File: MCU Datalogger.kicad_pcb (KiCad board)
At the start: 2 copper layers, 50 x 30 mm, 29 parts, among them J1 Conn_01x09_Male, J2 Conn_01x04_Male, J3 Conn_02x03_Odd_Even, J4 Conn_01x04_Male, U1 24LC1025, U2 DS1337S+, U3 24LC1025, U4 ATMEGA328P-AU, Y1 32.768 KHz, Y2 16MHz

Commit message: more routing/wiring
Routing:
- net GND: track 51.7 -> 62.3 mm, vias 6 -> 10
- net /Vcc: track 93.1 -> 95.7 mm, vias 3 -> 5
- added copper zone on F.Cu, net /Vcc
- added copper zone on B.Cu, net GND
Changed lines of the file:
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@@
   (segment (start 108.3564 83.491) (end 110.1598 85.2944) (width 0.25) (layer "B.Cu") (net 1))
   (segment (start 110.1598 85.2944) (end 110.1598 88.2904) (width 0.25) (layer "B.Cu") (net 1))
-  (segment (start 116.120715 81.5594) (end 116.2793 81.5594) (width 0.35) (layer "F.Cu") (net 2))
   (segment (start 110.2716 77.724) (end 110.2716 78.6486) (width 0.35) (layer "F.Cu") (net 2))
   (segment (start 80.01 86.482) (end 81.031 87.503) (width 0.35) (layer "F.Cu") (net 2))
+  (segment (start 91.992 78.6892) (end 94.869 78.6892) (width 0.35) (layer "F.Cu") (net 2))
   (segment (start 98.7146 77.4446) (end 100.7262 77.4446) (width 0.35) (layer "F.Cu") (net 2))
   (segment (start 78.735489 85.207489) (end 78.735489 82.667489) (width 0.35) (layer "F.Cu") (net 2))
   (segment (start 116.2558 98.5012) (end 116.2558 98.0694) (width 0.35) (layer "F.Cu") (net 2))
   (segment (start 85.663 94.8436) (end 87.249 94.8436) (width 0.35) (layer "F.Cu") (net 2))
+  (segment (start 97.064178 86.303) (end 96.60003 86.767148) (width 0.35) (layer "F.Cu") (net 2))
   (segment (start 87.5792 78.6892) (end 91.992 78.6892) (width 0.35) (layer "F.Cu") (net 2))
   (segment (start 120.2417 81.1511) (end 119.2784 80.1878) (width 0.35) (layer "F.Cu") (net 2))
   (segment (start 84.792 78.6892) (end 87.5792 78.6892) (width 0.35) (layer "F.Cu") (net 2))
+  (segment (start 97.0382 87.903) (end 96.60003 87.46483) (width 0.35) (layer "F.Cu") (net 2))
   (segment (start 116.2793 81.5594) (end 116.2793 80.9987) (width 0.35) (layer "F.Cu") (net 2))
   (segment (start 116.2558 98.5012) (end 116.2558 94.2086) (width 0.35) (layer "F.Cu") (net 2))
-  (segment (start 91.992 78.6892) (end 97.3684 78.6892) (width 0.35) (layer "F.Cu") (net 2))
   (segment (start 91.8904 84.963) (end 90.5764 84.963) (width 0.35) (layer "F.Cu") (net 2))
   (segment (start 81.031 87.503) (end 84.6904 87.503) (width 0.35) (layer "F.Cu") (net 2))
   (segment (start 87.5792 78.784493) (end 87.5792 78.6892) (width 0.35) (layer "F.Cu") (net 2))
+  (segment (start 98.1382 86.303) (end 97.064178 86.303) (width 0.35) (layer "F.Cu") (net 2))
   (segment (start 97.3684 78.6892) (end 98.6638 77.3938) (width 0.35) (layer "F.Cu") (net 2))
   (segment (start 84.792 81.2292) (end 85.134493 81.2292) (width 0.35) (layer "F.Cu") (net 2))
@@
   (segment (start 80.01 86.482) (end 78.735489 85.207489) (width 0.35) (layer "F.Cu") (net 2))
   (segment (start 120.2417 81.5594) (end 120.2417 81.1511) (width 0.35) (layer "F.Cu") (net 2))
+  (segment (start 96.60003 86.767148) (end 96.60003 87.15123) (width 0.35) (layer "F.Cu") (net 2))
+  (segment (start 106.7382 87.103) (end 108.3882 87.103) (width 0.35) (layer "F.Cu") (net 2))
   (segment (start 87.249 94.8436) (end 87.4776 94.615) (width 0.35) (layer "F.Cu") (net 2))
   (segment (start 116.2558 94.2086) (end 116.1796 94.1324) (width 0.35) (layer "F.Cu") (net 2))
+  (segment (start 94.869 78.6892) (end 97.3684 78.6892) (width 0.35) (layer "F.Cu") (net 2))
   (segment (start 80.173778 81.2292) (end 84.792 81.2292) (width 0.35) (layer "F.Cu") (net 2))
   (segment (start 78.735489 82.667489) (end 80.173778 81.2292) (width 0.35) (layer "F.Cu") (net 2))
@@
   (segment (start 90.5764 84.963) (end 90.297 84.6836) (width 0.35) (layer "F.Cu") (net 2))
   (segment (start 100.7262 77.4446) (end 100.8024 77.3684) (width 0.35) (layer "F.Cu") (net 2))
+  (segment (start 94.869 78.6892) (end 94.869 78.7654) (width 0.35) (layer "F.Cu") (net 2))
+  (segment (start 96.60003 87.46483) (end 96.60003 87.15123) (width 0.35) (layer "F.Cu") (net 2))
+  (segment (start 94.869 78.7654) (end 95.504 79.4004) (width 0.35) (layer "F.Cu") (net 2))
   (segment (start 98.6638 77.3938) (end 98.7146 77.4446) (width 0.35) (layer "F.Cu") (net 2))
   (segment (start 116.2793 80.9987) (end 115.5446 80.264) (width 0.35) (layer "F.Cu") (net 2))
   (segment (start 85.134493 81.2292) (end 87.5792 78.784493) (width 0.35) (layer "F.Cu") (net 2))
+  (segment (start 108.3882 87.103) (end 108.585 87.2998) (width 0.35) (layer "F.Cu") (net 2))
+  (segment (start 98.1382 87.903) (end 97.0382 87.903) (width 0.35) (layer "F.Cu") (net 2))
+  (via (at 123.7742 94.5388) (size 0.9) (drill 0.4) (layers "F.Cu" "B.Cu") (net 2))
+  (via (at 96.60003 87.15123) (size 0.9) (drill 0.4) (layers "F.Cu" "B.Cu") (net 2))
   (via (at 117.4242 96.901) (size 0.9) (drill 0.4) (layers "F.Cu" "B.Cu") (net 2))
   (via (at 110.6424 79.0194) (size 0.9) (drill 0.4) (layers "F.Cu" "B.Cu") (net 2))
@@
   (via (at 115.5446 80.264) (size 0.9) (drill 0.4) (layers "F.Cu" "B.Cu") (net 2))
   (via (at 87.4776 94.615) (size 0.9) (drill 0.4) (layers "F.Cu" "B.Cu") (net 2))
+  (via (at 108.585 87.2998) (size 0.9) (drill 0.4) (layers "F.Cu" "B.Cu") (net 2))
   (via (at 119.2784 80.1878) (size 0.9) (drill 0.4) (layers "F.Cu" "B.Cu") (net 2))
+  (via (at 95.504 79.4004) (size 0.9) (drill 0.4) (layers "F.Cu" "B.Cu") (net 2))
+  (segment (start 126.4158 91.9734) (end 123.8504 94.5388) (width 0.35) (layer "B.Cu") (net 2))
+  (segment (start 123.8504 94.5388) (end 123.7742 94.5388) (width 0.35) (layer "B.Cu") (net 2))
   (segment (start 126.4158 94.5134) (end 126.3396 94.5134) (width 0.35) (layer "F.Cu") (net 3))
   (segment (start 87.10128 101.084795) (end 87.496405 101.47992) (width 0.35) (layer "F.Cu") (net 3))
@@
   (segment (start 122.047 88.5698) (end 120.8551 88.5698) (width 0.35) (layer "F.Cu") (net 3))
   (segment (start 88.3412 83.693) (end 91.8904 83.693) (width 0.35) (layer "F.Cu") (net 3))
+  (via (at 88.5444 79.9592) (size 0.8) (drill 0.4) (layers "F.Cu" "B.Cu") (free) (net 3))
   (via (at 123.571 90.0938) (size 0.9) (drill 0.4) (layers "F.Cu" "B.Cu") (net 3))
   (via (at 124.2822 92.456) (size 0.9) (drill 0.4) (layers "F.Cu" "B.Cu") (net 3))
   (via (at 119.1006 84.0994) (size 0.9) (drill 0.4) (layers "F.Cu" "B.Cu") (net 3))
+  (via (at 88.4428 77.47) (size 0.8) (drill 0.4) (layers "F.Cu" "B.Cu") (free) (net 3))
   (segment (start 105.3338 104.267) (end 106.557511 105.490711) (width 0.35) (layer "B.Cu") (net 3))
   (segment (start 125.115889 95.813311) (end 126.4158 94.5134) (width 0.35) (layer "B.Cu") (net 3))
   (segment (start 119.1006 84.0994) (end 121.528511 81.671489) (width 0.35) (layer "B.Cu") (net 3))
   (segment (start 115.326 104.2162) (end 116.600511 105.490711) (width 0.35) (layer "B.Cu") (net 3))
+  (segment (start 88.4428 77.47) (end 88.4428 79.8576) (width 0.35) (layer "B.Cu") (net 3))
   (segment (start 125.115889 101.629911) (end 125.115889 95.813311) (width 0.35) (layer "B.Cu") (net 3))
   (segment (start 114.051489 105.490711) (end 115.326 104.2162) (width 0.35) (layer "B.Cu") (net 3))
+  (segment (start 88.4428 79.8576) (end 88.5444 79.9592) (width 0.35) (layer "B.Cu") (net 3))
   (segment (start 116.600511 105.490711) (end 121.255089 105.490711) (width 0.35) (layer "B.Cu") (net 3))
   (segment (start 121.255089 105.490711) (end 125.115889 101.629911) (width 0.35) (layer "B.Cu") (net 3))
@@
   (segment (start 123.9978 82.946) (end 122.823289 84.120511) (width 0.25) (layer "B.Cu") (net 30))
   (segment (start 122.823289 89.596911) (end 121.8184 90.6018) (width 0.25) (layer "B.Cu") (net 30))
+  (zone (net 3) (net_name "/Vcc") (layer "F.Cu") (hatch edge 0.508)
+    (connect_pads (clearance 0.508))
+    (min_thickness 0.254) (filled_areas_thickness no)
+    (fill yes (thermal_gap 0.508) (thermal_bridge_width 0.508))
+    (polygon
+      (pts
+        (xy 123.825 78.3336)
+        (xy 123.9266 79.0448)
+        (xy 124.5362 80.0354)
+        (xy 125.603 80.518)
+        (xy 128.1938 80.4418)
+        (xy 128.1938 101.4476)
+        (xy 126.9492 101.5238)
+        (xy 125.7808 101.4476)
+        (xy 124.6886 101.7778)
+        (xy 123.698 102.8954)
+        (xy 123.4948 106.0196)
+        (xy 82.2706 106.0196)
+        (xy 82.6516 104.902)
+        (xy 82.931 104.0892)
+        (xy 82.8802 103.3018)
+        (xy 82.677 102.743)
+        (xy 82.2452 102.1334)
+        (xy 81.661 101.6762)
+        (xy 80.899 101.3968)
+        (xy 80.0354 101.4476)
+        (xy 78.3336 101.9556)
+        (xy 78.3336 81.7626)
+        (xy 78.359 79.9846)
+        (xy 79.4512 80.7974)
+        (xy 81.3816 80.772)
+        (xy 82.9564 79.375)
+        (xy 83.0326 76.2254)
+        (xy 83.0326 76.2508)
+        (xy 83.058 76.1492)
+        (xy 124.0028 76.1492)
+      )
+    )
+  )
+  (zone (net 2) (net_name "GND") (layer "B.Cu") (hatch edge 0.508)
+    (connect_pads (clearance 0.508))
+    (min_thickness 0.254) (filled_areas_thickness no)
+    (fill yes (thermal_gap 0.508) (thermal_bridge_width 0.508))
+    (polygon
+      (pts
+        (xy 123.825 78.3336)
+        (xy 123.9266 79.0448)
+        (xy 124.5362 80.0354)
+        (xy 125.603 80.518)
+        (xy 128.1938 80.4418)
+        (xy 128.1938 101.4476)
+        (xy 126.9492 101.5238)
+        (xy 125.7808 101.4476)
+        (xy 124.6886 101.7778)
+        (xy 123.698 102.8954)
+        (xy 123.4948 106.0196)
+        (xy 82.2706 106.0196)
+        (xy 82.6516 104.902)
+        (xy 82.931 104.0892)
+        (xy 82.8802 103.3018)
+        (xy 82.677 102.743)
+        (xy 82.2452 102.1334)
+        (xy 81.661 101.6762)
+        (xy 80.899 101.3968)
+        (xy 80.0354 101.4476)
+        (xy 78.3336 101.9556)
+        (xy 78.3336 81.7626)
+        (xy 78.359 79.9846)
+        (xy 79.4512 80.7974)
+        (xy 81.3816 80.772)
+        (xy 82.9564 79.375)
+        (xy 83.0326 76.2254)
+        (xy 83.0326 76.2508)
+        (xy 83.058 76.1492)
+        (xy 124.0028 76.1492)
+      )
+    )
+  )
 )

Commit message: completed routing
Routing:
- net GND: track 62.3 -> 58.6 mm, vias 10 -> 9
- net /Vcc: track 95.7 -> 97.1 mm

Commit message: ready to start on the silk screen
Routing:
- net /Vcc: track 97.1 -> 114.4 mm, vias 5 -> 6
- net /SDA: track 62.6 -> 63.9 mm
- net /D3: track 24.5 -> 25.2 mm

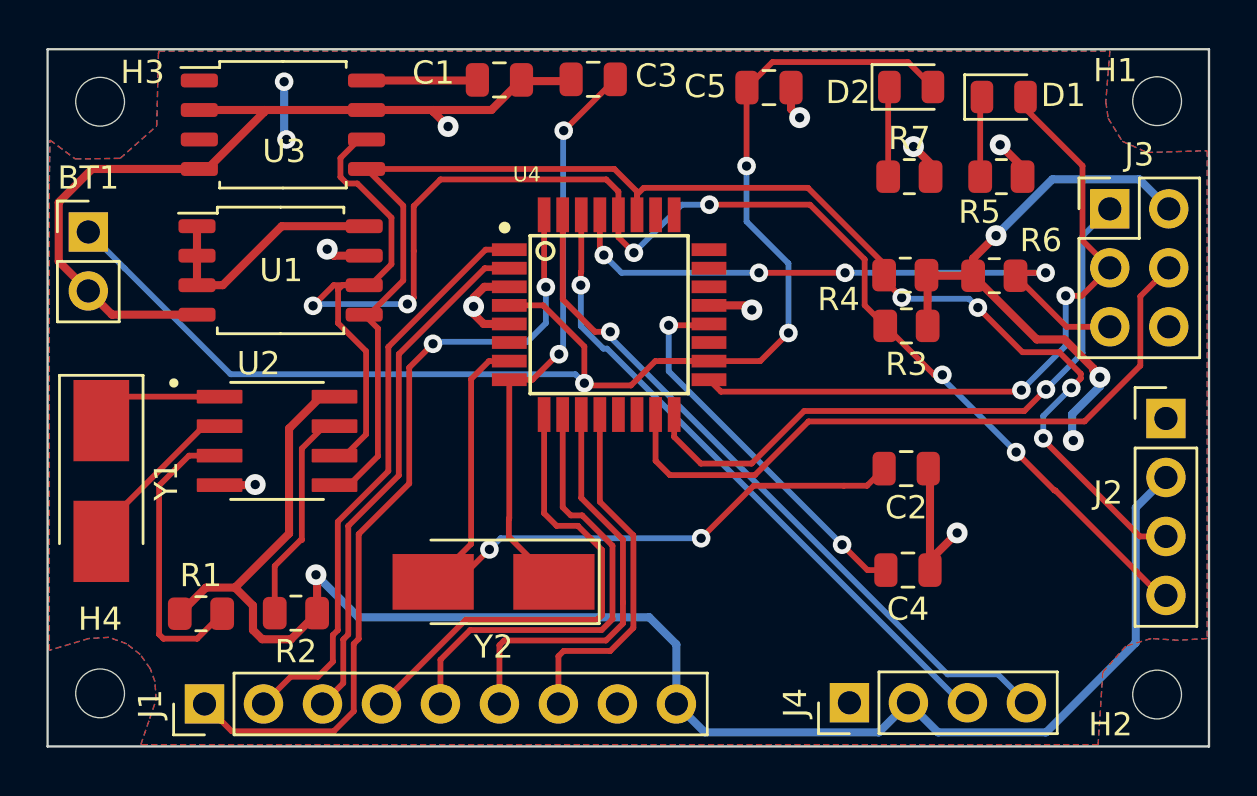
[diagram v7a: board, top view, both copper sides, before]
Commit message: Post fixing the schematic for the missing vcc net and the pcb resulting changes
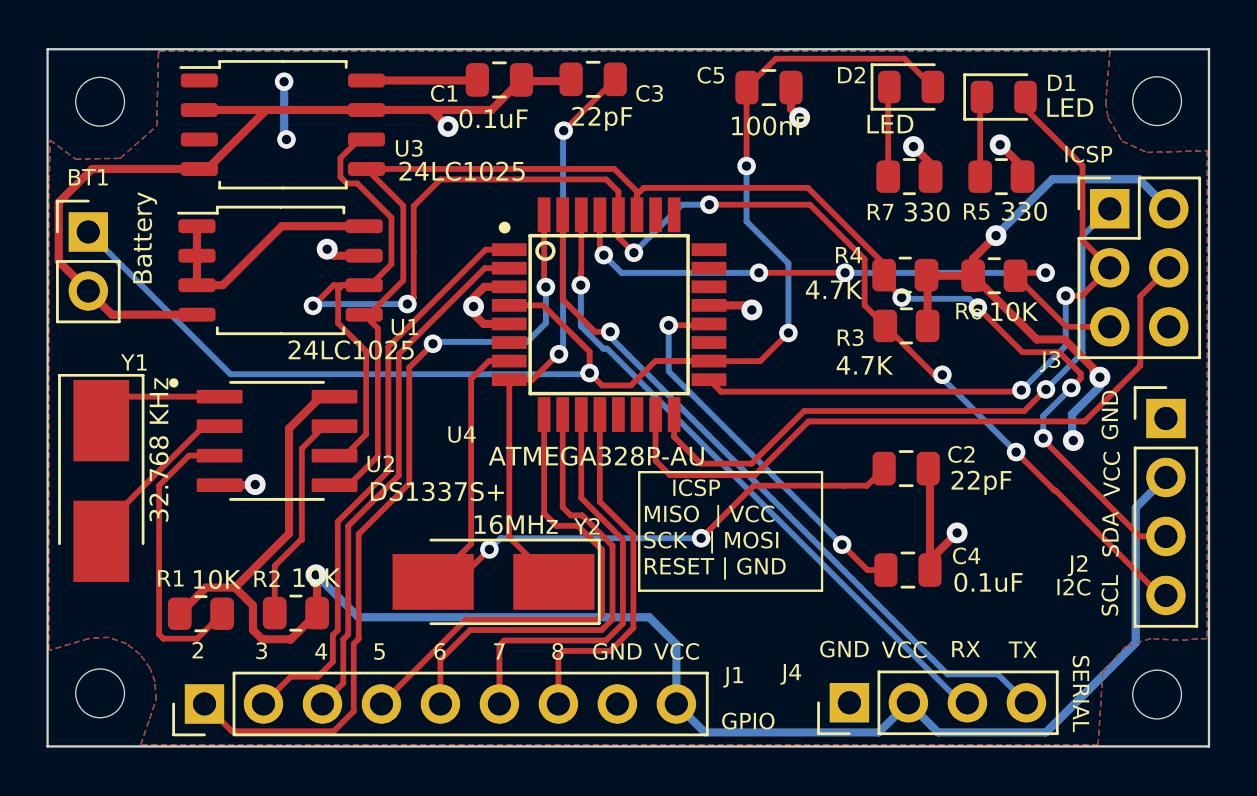
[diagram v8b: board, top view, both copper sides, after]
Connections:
- BT1 pad 1: Net-(BT1-Pad1) -> /Vcc
- C5 pad 1: Net-(BT1-Pad1) -> /Vcc
- D2 pad 2: Net-(BT1-Pad1) -> /Vcc
- U4 pad 18: Net-(BT1-Pad1) -> /Vcc
- U4 pad 4: Net-(BT1-Pad1) -> /Vcc
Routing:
- net Net-(BT1-Pad1): track 61.7 -> 0.00 mm, vias 3 -> 0
- net /Vcc: track 114.4 -> 175.9 mm, vias 6 -> 9
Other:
- board text added: "2"
- board text added: "3"
- board text added: "4"
- board text added: "5"
- board text added: "6"
- board text added: "7"
- board text added: "8"
- board text added: "GND"
- board text added: "GPIO"
- board text added: "I2C"
- board text added: "ICSP"
- board text added: "ICSP MISO | VCC SCK | MOSI RESET | GND"
- board text added: "RX"
- board text added: "SCL"
- board text added: "SDA"
- board text added: "SERIAL"
- board text added: "TX"
- board text added: "VCC"
